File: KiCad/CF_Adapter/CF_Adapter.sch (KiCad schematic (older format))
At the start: 3 parts, among them J1 Z-Fighter IDE Connector, J2 CF Card Socket

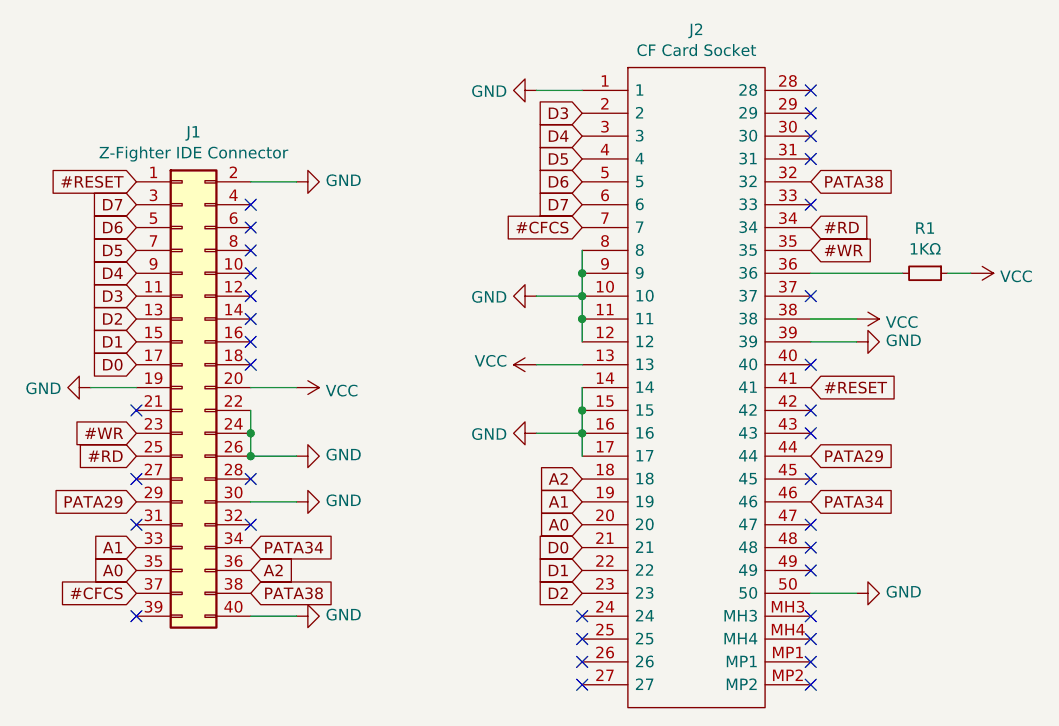
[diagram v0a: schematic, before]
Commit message: Changed schematic CF connector
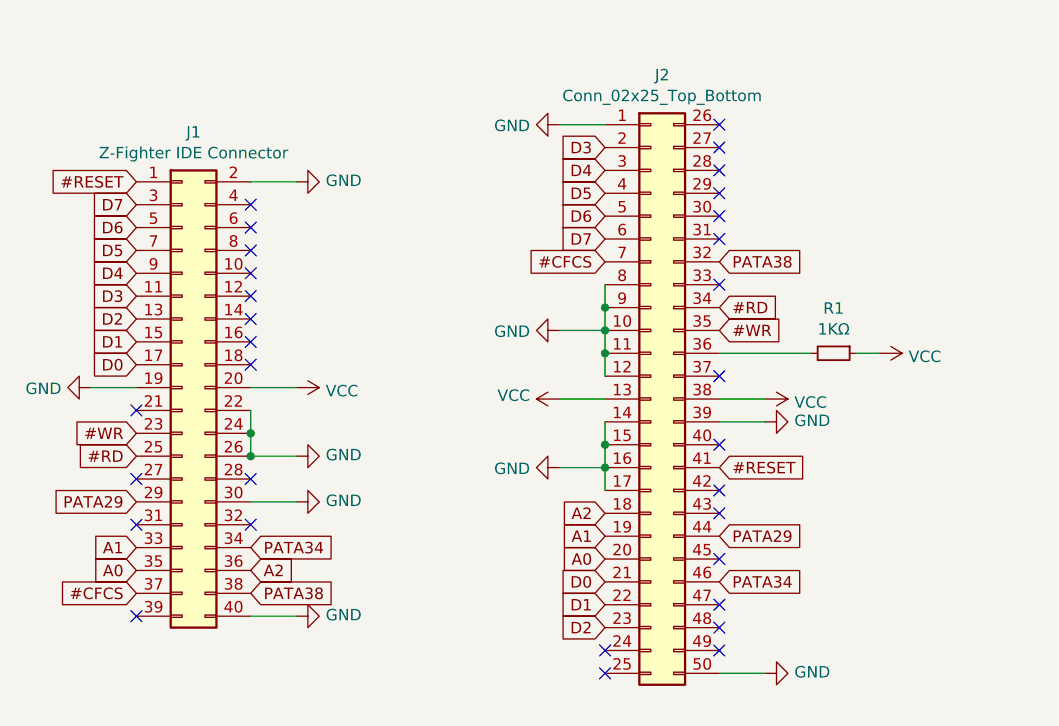
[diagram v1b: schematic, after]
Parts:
- removed J2: CF Card Socket, Connector_Card:315610050210871, symbol 315610050210871+:315610050210871+
- added J2: Conn_02x25_Top_Bottom, Connector_Card:CF-Card_3M_N7E50-7516PK-20-WF, symbol Connector_Generic:Conn_02x25_Top_Bottom
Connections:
- net #CFCS: now also J2.7 (Pin_7)
- net #RD: now also J2.34 (Pin_34)
- net #RESET: now also J2.41 (Pin_41)
- net #WR: now also J2.35 (Pin_35)
- net A0: now also J2.20 (Pin_20)
- net A1: now also J2.19 (Pin_19)
- net A2: now also J2.18 (Pin_18)
- net D0: now also J2.21 (Pin_21)
- net D1: now also J2.22 (Pin_22)
- net D2: now also J2.23 (Pin_23)
- net D3: now also J2.2 (Pin_2)
- net D4: now also J2.3 (Pin_3)
- net D5: now also J2.4 (Pin_4)
- net D6: now also J2.5 (Pin_5)
- net D7: now also J2.6 (Pin_6)
- net GND: now also J2.1 (Pin_1), J2.10 (Pin_10), J2.11 (Pin_11), J2.12 (Pin_12), J2.14 (Pin_14), J2.15 (Pin_15), J2.16 (Pin_16), J2.17 (Pin_17), J2.39 (Pin_39), J2.50 (Pin_50), J2.8 (Pin_8), J2.9 (Pin_9)
- net PATA29: now also J2.44 (Pin_44)
- net PATA34: now also J2.46 (Pin_46)
- net PATA38: now also J2.32 (Pin_32)
- net VCC: now also J2.13 (Pin_13), J2.38 (Pin_38)
- net at R1.2: now also J2.36 (Pin_36)
- no-connect marks 35 -> 31
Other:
- moved on the sheet: R1
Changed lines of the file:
@@
 $EndDescr
-$Comp
-L 315610050210871+:315610050210871+ J2
-U 1 1 618DDEDC
-P 7050 3600
-F 0 "J2" H 7050 5065 50  0000 C CNN
-F 1 "CF Card Socket" H 7050 4974 50  0000 C CNN
-F 2 "Connector_Card:315610050210871" H 6700 5000 50  0001 L CNN
-F 3 "" H 7400 4800 50  0001 L CNN
-	1    7050 3600
-	1    0    0    -1
-$EndComp
 $Comp
 L Connector_Generic:Conn_02x20_Odd_Even J1
@@
 L power:VCC #PWR0107
 U 1 1 618FAAD4
-P 7750 3400
-F 0 "#PWR0107" H 7750 3250 50  0001 C CNN
-F 1 "VCC" V 7765 3528 50  0000 L CNN
-F 2 "" H 7750 3400 50  0001 C CNN
-F 3 "" H 7750 3400 50  0001 C CNN
-	1    7750 3400
-	0    1    1    0
-$EndComp
-Wire Wire Line
-	7750 3400 7550 3400
-Text GLabel 6550 4400 0    50   Input ~ 0
+P 7350 3750
+F 0 "#PWR0107" H 7350 3600 50  0001 C CNN
+F 1 "VCC" V 7365 3878 50  0000 L CNN
+F 2 "" H 7350 3750 50  0001 C CNN
+F 3 "" H 7350 3750 50  0001 C CNN
+	1    7350 3750
+	0    1    1    0
+$EndComp
+Wire Wire Line
+	7350 3750 7150 3750
+Text GLabel 6650 4550 0    50   Input ~ 0
 D0
-Text GLabel 6550 4500 0    50   Input ~ 0
+Text GLabel 6650 4650 0    50   Input ~ 0
 D1
-Text GLabel 6550 4600 0    50   Input ~ 0
+Text GLabel 6650 4750 0    50   Input ~ 0
 D2
-Text GLabel 6550 2500 0    50   Input ~ 0
-D3
-Text GLabel 6550 2600 0    50   Input ~ 0
-D4
-Text GLabel 6550 2700 0    50   Input ~ 0
-D5
-Text GLabel 6550 2800 0    50   Input ~ 0
-D6
-Text GLabel 6550 2900 0    50   Input ~ 0
-D7
-Text GLabel 6550 3000 0    50   Input ~ 0
-#CFCS
-Wire Wire Line
-	6550 3100 6550 3200
-Connection ~ 6550 3200
-Wire Wire Line
-	6550 3200 6550 3300
-Connection ~ 6550 3300
-Wire Wire Line
-	6550 3300 6550 3400
-Connection ~ 6550 3400
-Wire Wire Line
-	6550 3400 6550 3500
 $Comp
 L power:VCC #PWR0108
 U 1 1 61902FCD
-P 6350 3600
-F 0 "#PWR0108" H 6350 3450 50  0001 C CNN
-F 1 "VCC" V 6365 3728 50  0000 L CNN
-F 2 "" H 6350 3600 50  0001 C CNN
-F 3 "" H 6350 3600 50  0001 C CNN
-	1    6350 3600
-	0    -1   -1   0
-$EndComp
-Wire Wire Line
-	6350 3600 6550 3600
+P 6450 3750
+F 0 "#PWR0108" H 6450 3600 50  0001 C CNN
+F 1 "VCC" V 6465 3878 50  0000 L CNN
+F 2 "" H 6450 3750 50  0001 C CNN
+F 3 "" H 6450 3750 50  0001 C CNN
+	1    6450 3750
+	0    -1   -1   0
+$EndComp
+Wire Wire Line
+	6450 3750 6650 3750
 $Comp
 L power:GND #PWR0109
 U 1 1 6190381C
-P 6350 3300
-F 0 "#PWR0109" H 6350 3050 50  0001 C CNN
-F 1 "GND" V 6355 3172 50  0000 R CNN
-F 2 "" H 6350 3300 50  0001 C CNN
-F 3 "" H 6350 3300 50  0001 C CNN
-	1    6350 3300
-	0    1    1    0
-$EndComp
-Wire Wire Line
-	6350 3300 6550 3300
-Wire Wire Line
-	6550 3700 6550 3800
-Connection ~ 6550 3800
-Wire Wire Line
-	6550 3800 6550 3900
-Connection ~ 6550 3900
-Wire Wire Line
-	6550 3900 6550 4000
+P 6450 3450
+F 0 "#PWR0109" H 6450 3200 50  0001 C CNN
+F 1 "GND" V 6455 3322 50  0000 R CNN
+F 2 "" H 6450 3450 50  0001 C CNN
+F 3 "" H 6450 3450 50  0001 C CNN
+	1    6450 3450
+	0    1    1    0
+$EndComp
+Wire Wire Line
+	6450 3450 6650 3450
 $Comp
 L power:GND #PWR0110
 U 1 1 61905730
-P 6350 3900
-F 0 "#PWR0110" H 6350 3650 50  0001 C CNN
-F 1 "GND" V 6355 3772 50  0000 R CNN
-F 2 "" H 6350 3900 50  0001 C CNN
-F 3 "" H 6350 3900 50  0001 C CNN
-	1    6350 3900
-	0    1    1    0
-$EndComp
-Wire Wire Line
-	6350 3900 6550 3900
-Text GLabel 6550 4100 0    50   Input ~ 0
+P 6450 4050
+F 0 "#PWR0110" H 6450 3800 50  0001 C CNN
+F 1 "GND" V 6455 3922 50  0000 R CNN
+F 2 "" H 6450 4050 50  0001 C CNN
+F 3 "" H 6450 4050 50  0001 C CNN
+	1    6450 4050
+	0    1    1    0
+$EndComp
+Wire Wire Line
+	6450 4050 6650 4050
+Text GLabel 6650 4250 0    50   Input ~ 0
 A2
-Text GLabel 6550 4200 0    50   Input ~ 0
+Text GLabel 6650 4350 0    50   Input ~ 0
 A1
-Text GLabel 6550 4300 0    50   Input ~ 0
+Text GLabel 6650 4450 0    50   Input ~ 0
 A0
-NoConn ~ 6550 4700
-NoConn ~ 6550 4800
+Wire Wire Line
+	6650 2550 6450 2550
+Wire Wire Line
+	7350 4950 7150 4950
+$Comp
+L power:GND #PWR0113
+U 1 1 6190D69F
+P 7350 3850
+F 0 "#PWR0113" H 7350 3600 50  0001 C CNN
+F 1 "GND" V 7355 3722 50  0000 R CNN
+F 2 "" H 7350 3850 50  0001 C CNN
+F 3 "" H 7350 3850 50  0001 C CNN
+	1    7350 3850
+	0    -1   -1   0
+$EndComp
+Wire Wire Line
+	7350 3850 7150 3850
+Text GLabel 7150 4050 2    50   Input ~ 0
+#RESET
+Text GLabel 7150 4350 2    50   Input ~ 0
+PATA29
+Text GLabel 7150 4550 2    50   Input ~ 0
+PATA34
+Text GLabel 7150 3150 2    50   Input ~ 0
+PATA38
+Text GLabel 7150 3350 2    50   Input ~ 0
+#RD
+Text GLabel 7150 3450 2    50   Input ~ 0
+#WR
+Wire Wire Line
+	7150 3550 7550 3550
+$Comp
+L power:VCC #PWR0114
+U 1 1 619172C7
+P 7850 3550
+F 0 "#PWR0114" H 7850 3400 50  0001 C CNN
+F 1 "VCC" V 7865 3678 50  0000 L CNN
+F 2 "" H 7850 3550 50  0001 C CNN
+F 3 "" H 7850 3550 50  0001 C CNN
+	1    7850 3550
+	0    1    1    0
+$EndComp
+Wire Wire Line
+	7750 3550 7850 3550
+$Comp
+L Device:R_Small R1
+U 1 1 61915306
+P 7650 3550
+F 0 "R1" V 7454 3550 50  0000 C CNN
+F 1 "1KΩ" V 7545 3550 50  0000 C CNN
+F 2 "Resistor_SMD:R_1206_3216Metric_Pad1.30x1.75mm_HandSolder" V 7546 3550 50  0001 C CNN
+F 3 "~" H 7650 3550 50  0001 C CNN
+	1    7650 3550
+	0    1    1    0
+$EndComp
+$Comp
+L Connector_Generic:Conn_02x25_Top_Bottom J2
+U 1 1 61A451DC
+P 6850 3750
+F 0 "J2" H 6900 5167 50  0000 C CNN
+F 1 "Conn_02x25_Top_Bottom" H 6900 5076 50  0000 C CNN
+F 2 "Connector_Card:CF-Card_3M_N7E50-7516PK-20-WF" H 6850 3750 50  0001 C CNN
+F 3 "~" H 6850 3750 50  0001 C CNN
+	1    6850 3750
+	1    0    0    -1
+$EndComp
+NoConn ~ 6650 4850
+NoConn ~ 6650 4950
+NoConn ~ 7150 2550
+NoConn ~ 7150 2650
+NoConn ~ 7150 2750
+NoConn ~ 7150 2850
+NoConn ~ 7150 2950
+NoConn ~ 7150 3050
+NoConn ~ 7150 3250
+NoConn ~ 7150 3650
+NoConn ~ 7150 3950
+NoConn ~ 7150 4150
+NoConn ~ 7150 4250
+NoConn ~ 7150 4450
+NoConn ~ 7150 4650
+NoConn ~ 7150 4750
+NoConn ~ 7150 4850
+$Comp
+L power:GND #PWR0112
+U 1 1 6190A72B
+P 7350 4950
+F 0 "#PWR0112" H 7350 4700 50  0001 C CNN
+F 1 "GND" V 7355 4822 50  0000 R CNN
+F 2 "" H 7350 4950 50  0001 C CNN
+F 3 "" H 7350 4950 50  0001 C CNN
+	1    7350 4950
+	0    -1   -1   0
+$EndComp
 $Comp
 L power:GND #PWR0111
 U 1 1 61907DA0
-P 6350 2400
-F 0 "#PWR0111" H 6350 2150 50  0001 C CNN
-F 1 "GND" V 6355 2272 50  0000 R CNN
-F 2 "" H 6350 2400 50  0001 C CNN
-F 3 "" H 6350 2400 50  0001 C CNN
-	1    6350 2400
-	0    1    1    0
-$EndComp
-Wire Wire Line
-	6550 2400 6350 2400
-$Comp
-L power:GND #PWR0112
-U 1 1 6190A72B
-P 7750 4600
-F 0 "#PWR0112" H 7750 4350 50  0001 C CNN
-F 1 "GND" V 7755 4472 50  0000 R CNN
-F 2 "" H 7750 4600 50  0001 C CNN
-F 3 "" H 7750 4600 50  0001 C CNN
-	1    7750 4600
-	0    -1   -1   0
-$EndComp
-Wire Wire Line
-	7750 4600 7550 4600
-NoConn ~ 7550 4500
-NoConn ~ 7550 4400
-NoConn ~ 7550 4300
-NoConn ~ 6550 4900
-NoConn ~ 6550 5000
-NoConn ~ 7550 2400
-NoConn ~ 7550 2500
-NoConn ~ 7550 2600
-NoConn ~ 7550 2700
-NoConn ~ 7550 2900
-NoConn ~ 7550 3300
-NoConn ~ 7550 3600
-NoConn ~ 7550 3800
-NoConn ~ 7550 3900
-$Comp
-L power:GND #PWR0113
-U 1 1 6190D69F
-P 7750 3500
-F 0 "#PWR0113" H 7750 3250 50  0001 C CNN
-F 1 "GND" V 7755 3372 50  0000 R CNN
-F 2 "" H 7750 3500 50  0001 C CNN
-F 3 "" H 7750 3500 50  0001 C CNN
-	1    7750 3500
-	0    -1   -1   0
-$EndComp
-Wire Wire Line
-	7750 3500 7550 3500
-NoConn ~ 7550 4100
-Text GLabel 7550 3700 2    50   Input ~ 0
-#RESET
-NoConn ~ 7550 4700
-NoConn ~ 7550 4800
-NoConn ~ 7550 4900
-NoConn ~ 7550 5000
-Text GLabel 7550 4000 2    50   Input ~ 0
-PATA29
-Text GLabel 7550 4200 2    50   Input ~ 0
-PATA34
-Text GLabel 7550 2800 2    50   Input ~ 0
-PATA38
-Text GLabel 7550 3000 2    50   Input ~ 0
-#RD
-Text GLabel 7550 3100 2    50   Input ~ 0
-#WR
-Wire Wire Line
-	7550 3200 7950 3200
-$Comp
-L power:VCC #PWR0114
-U 1 1 619172C7
-P 8250 3200
-F 0 "#PWR0114" H 8250 3050 50  0001 C CNN
-F 1 "VCC" V 8265 3328 50  0000 L CNN
-F 2 "" H 8250 3200 50  0001 C CNN
-F 3 "" H 8250 3200 50  0001 C CNN
-	1    8250 3200
-	0    1    1    0
-$EndComp
-Wire Wire Line
-	8150 3200 8250 3200
-$Comp
-L Device:R_Small R1
-U 1 1 61915306
-P 8050 3200
-F 0 "R1" V 7854 3200 50  0000 C CNN
-F 1 "1KΩ" V 7945 3200 50  0000 C CNN
-F 2 "Resistor_SMD:R_1206_3216Metric_Pad1.30x1.75mm_HandSolder" V 7946 3200 50  0001 C CNN
-F 3 "~" H 8050 3200 50  0001 C CNN
-	1    8050 3200
-	0    1    1    0
-$EndComp
+P 6450 2550
+F 0 "#PWR0111" H 6450 2300 50  0001 C CNN
+F 1 "GND" V 6455 2422 50  0000 R CNN
+F 2 "" H 6450 2550 50  0001 C CNN
+F 3 "" H 6450 2550 50  0001 C CNN
+	1    6450 2550
+	0    1    1    0
+$EndComp
+Text GLabel 6650 3150 0    50   Input ~ 0
+#CFCS
+Text GLabel 6650 3050 0    50   Input ~ 0
+D7
+Text GLabel 6650 2950 0    50   Input ~ 0
+D6
+Text GLabel 6650 2850 0    50   Input ~ 0
+D5
+Text GLabel 6650 2750 0    50   Input ~ 0
+D4
+Text GLabel 6650 2650 0    50   Input ~ 0
+D3
+Wire Wire Line
+	6650 3850 6650 3950
+Connection ~ 6650 3950
+Wire Wire Line
+	6650 3950 6650 4050
+Connection ~ 6650 4050
+Wire Wire Line
+	6650 4050 6650 4150
+Wire Wire Line
+	6650 3350 6650 3450
+Connection ~ 6650 3450
+Wire Wire Line
+	6650 3450 6650 3550
+Connection ~ 6650 3550
+Wire Wire Line
+	6650 3550 6650 3650
+Wire Wire Line
+	6650 3250 6650 3350
+Connection ~ 6650 3350
 $EndSCHEMATC
